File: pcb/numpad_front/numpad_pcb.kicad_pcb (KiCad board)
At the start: 2 copper layers, 56 parts, among them J1 Conn_01x16_Female

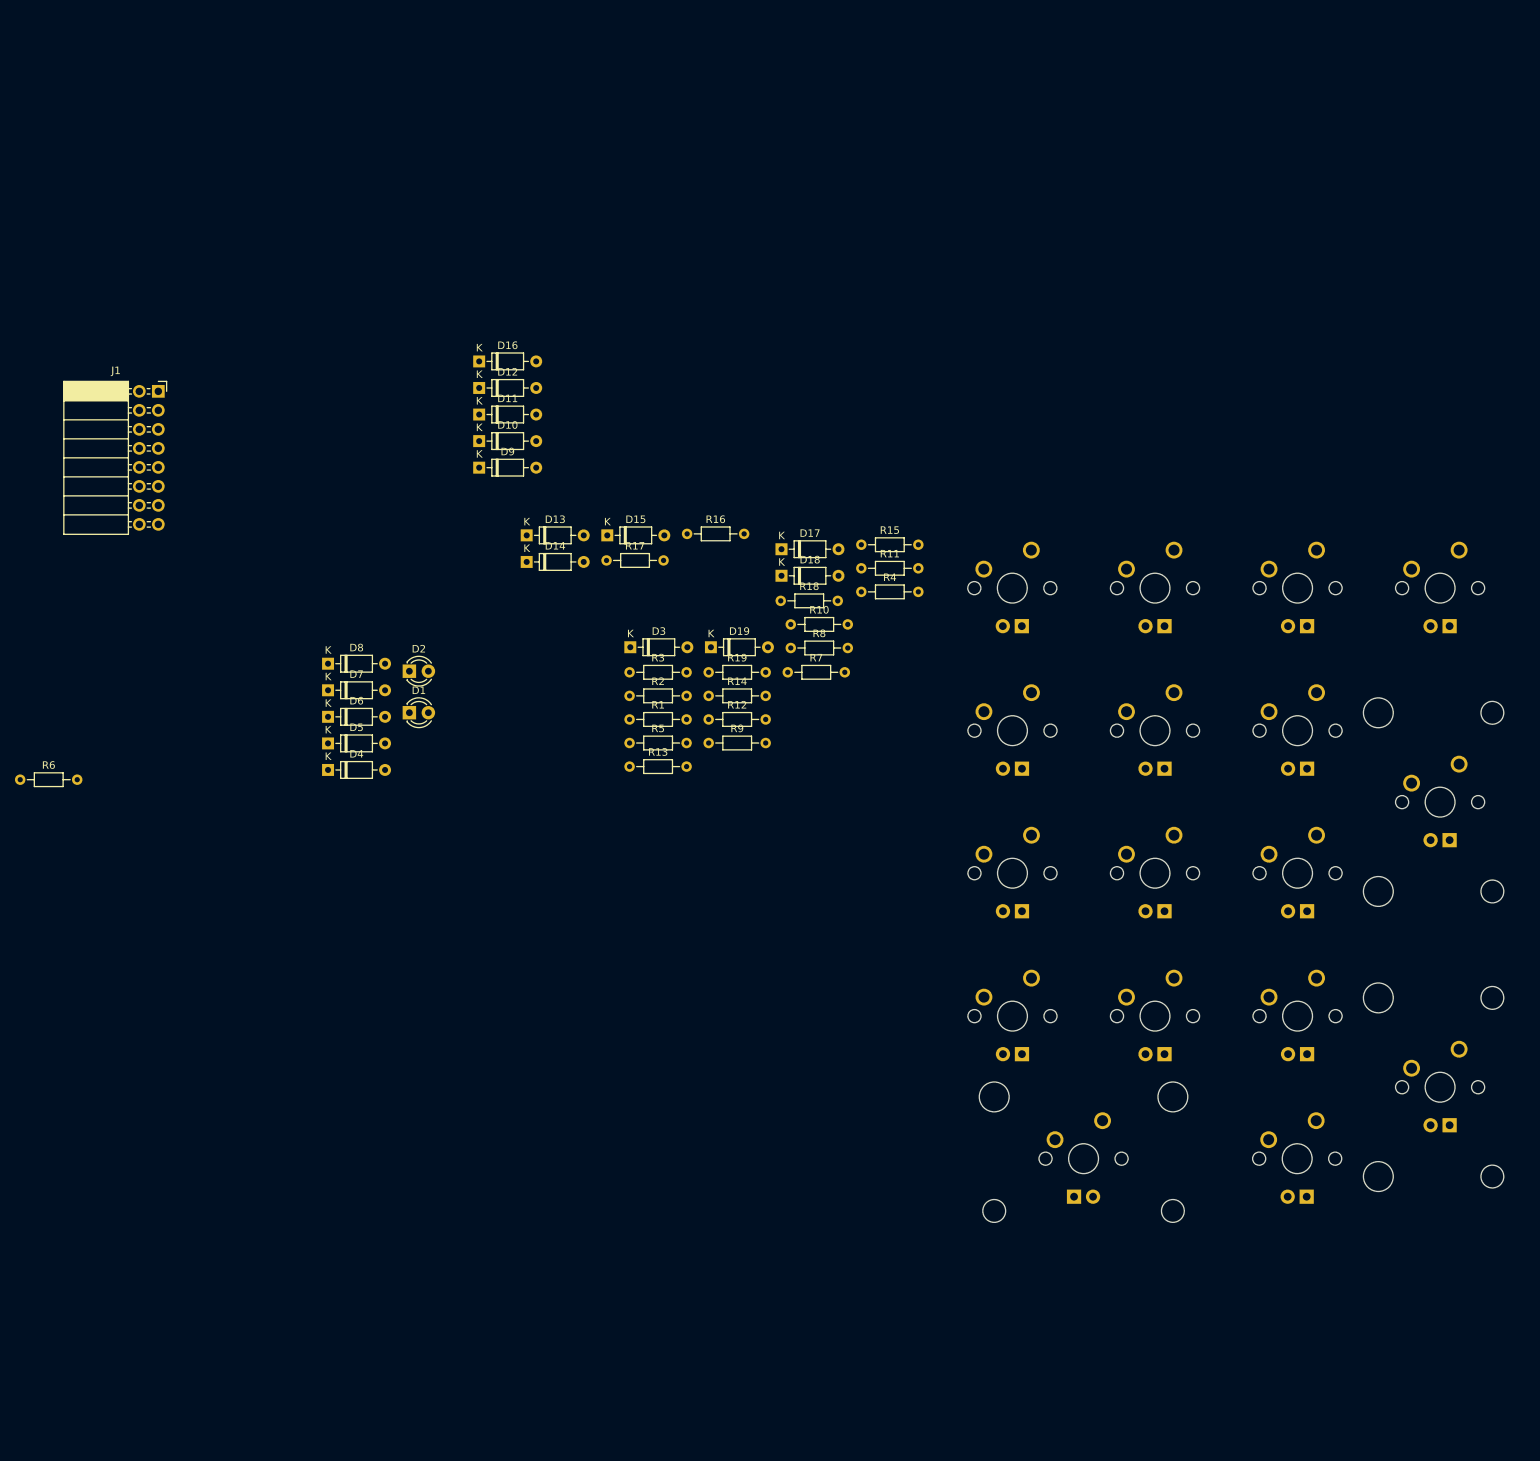
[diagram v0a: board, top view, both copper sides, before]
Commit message: Finish layout for numpad PCB
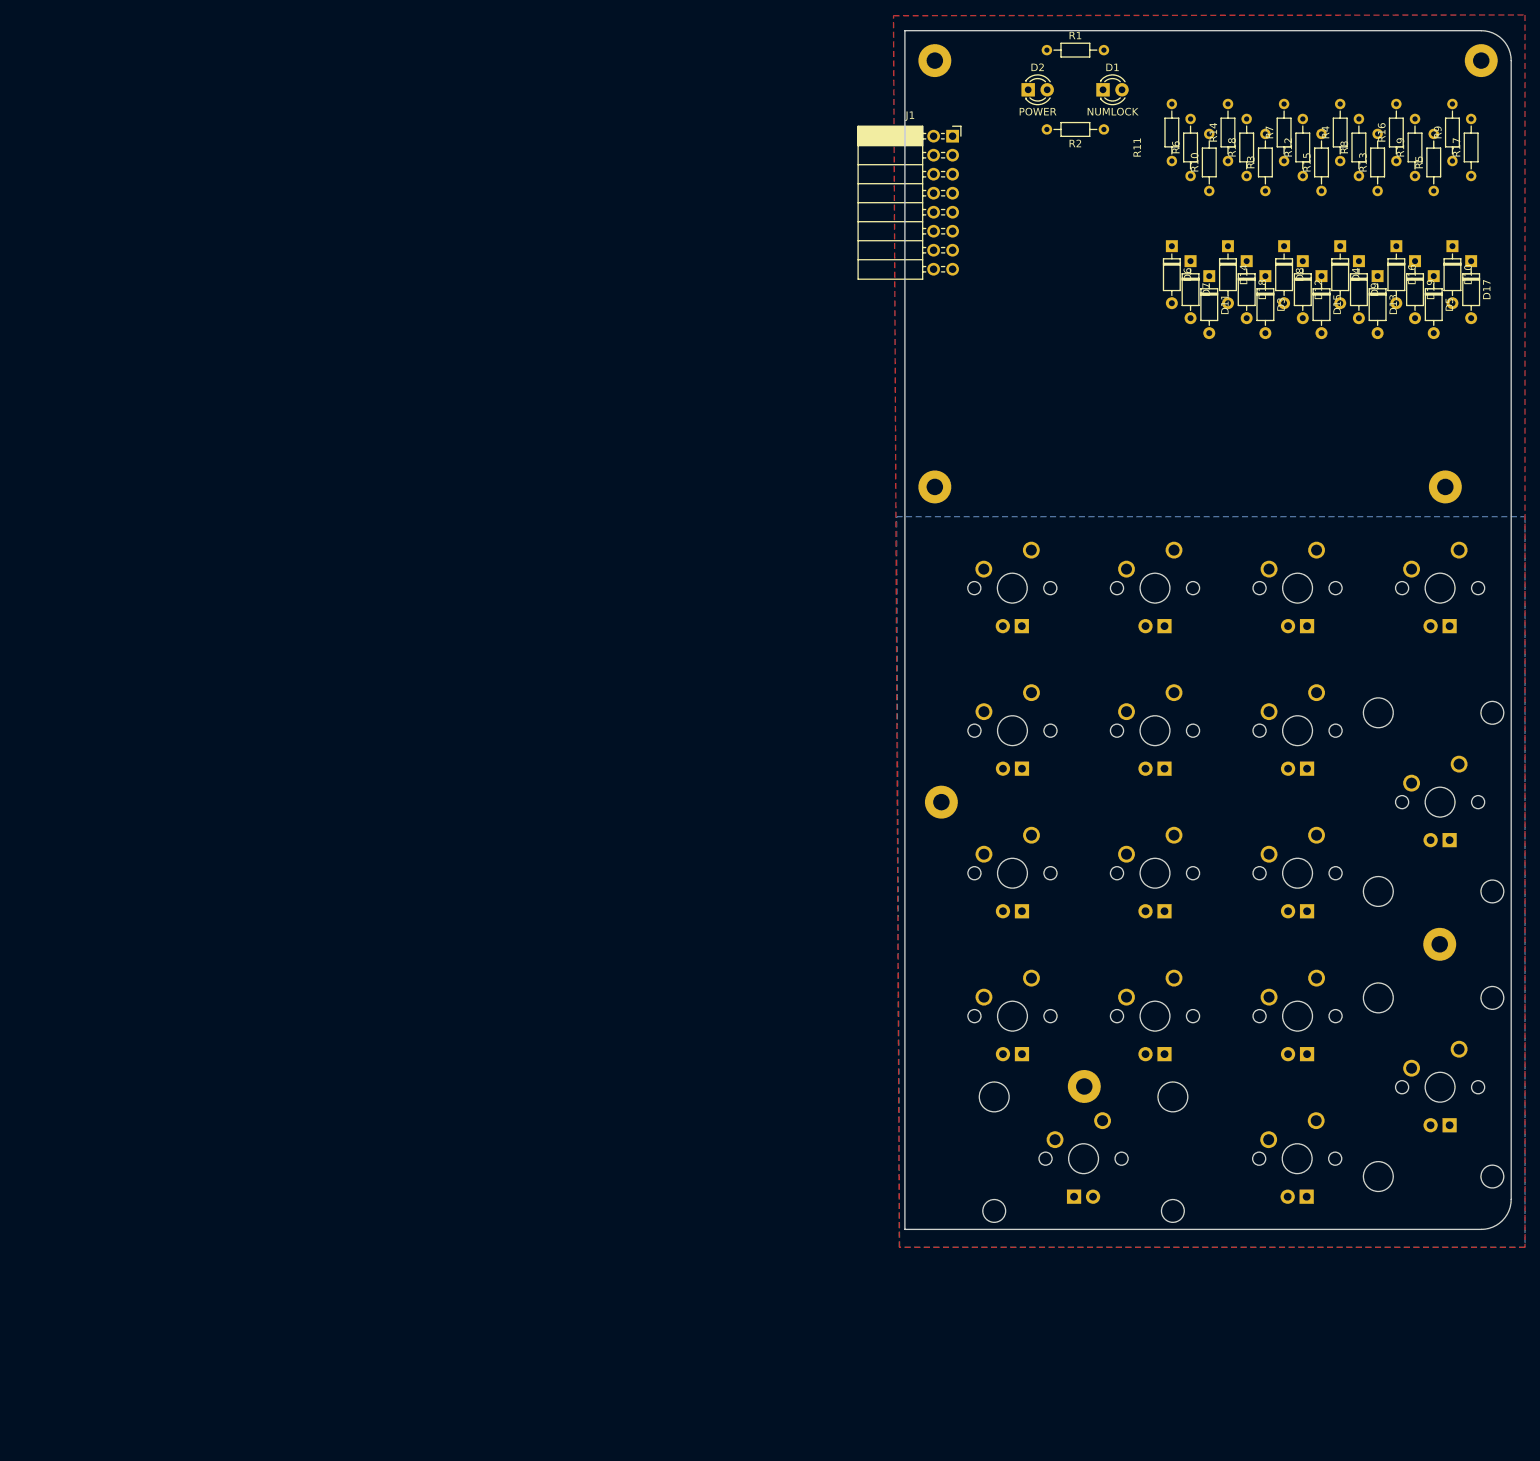
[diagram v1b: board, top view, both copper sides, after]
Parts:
- added REF**: MountingHole_2.2mm_M2_Pad, MountingHole:MountingHole_2.2mm_M2_Pad, F.Cu at (140.5, 3.40)
- added REF** (x2): MountingHole_2.2mm_M2_Pad, MountingHole:MountingHole_2.2mm_M2_Pad, F.Cu at (140.5, 60.4)
- added REF**: MountingHole_2.2mm_M2_Pad, MountingHole:MountingHole_2.2mm_M2_Pad, F.Cu at (141.4, 102.5)
- added REF**: MountingHole_2.2mm_M2_Pad, MountingHole:MountingHole_2.2mm_M2_Pad, F.Cu at (160.5, 140.5)
- added REF**: MountingHole_2.2mm_M2_Pad, MountingHole:MountingHole_2.2mm_M2_Pad, F.Cu at (208.0, 121.5)
- added REF**: MountingHole_2.2mm_M2_Pad, MountingHole:MountingHole_2.2mm_M2_Pad, F.Cu at (213.6, 3.40)
- moved R6 176.0 mm to (174.7, 18.8), turned to 90 degrees
- moved D5 160.4 mm to (207.2, 32.2), turned to 270 degrees
- moved D4 152.3 mm to (194.7, 28.2), turned to 270 degrees
- moved D8 139.4 mm to (187.2, 28.2), turned to 270 degrees
- moved D10 132.7 mm to (209.7, 28.2), turned to 270 degrees
- moved R5 130.4 mm to (207.2, 20.8), turned to 90 degrees
- moved D6 129.1 mm to (172.2, 28.2), turned to 270 degrees
- moved D7 128.7 mm to (174.7, 30.2), turned to 270 degrees
- moved R17 126.5 mm to (212.2, 18.8), turned to 90 degrees
- moved R9 126.2 mm to (209.7, 16.8), turned to 90 degrees
- moved R13 126.1 mm to (199.7, 20.8), turned to 90 degrees
- moved D1 124.6 mm to (163.0, 7.30)
- moved D16 123.5 mm to (202.2, 28.2), turned to 270 degrees
- moved D9 120.8 mm to (197.2, 30.2), turned to 270 degrees
- moved D13 118.9 mm to (199.7, 32.2), turned to 270 degrees
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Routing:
- added copper zone on F.Cu, net GND
- added copper zone on B.Cu, net LEDGND
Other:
- board outline added: 81 x 160.2 mm

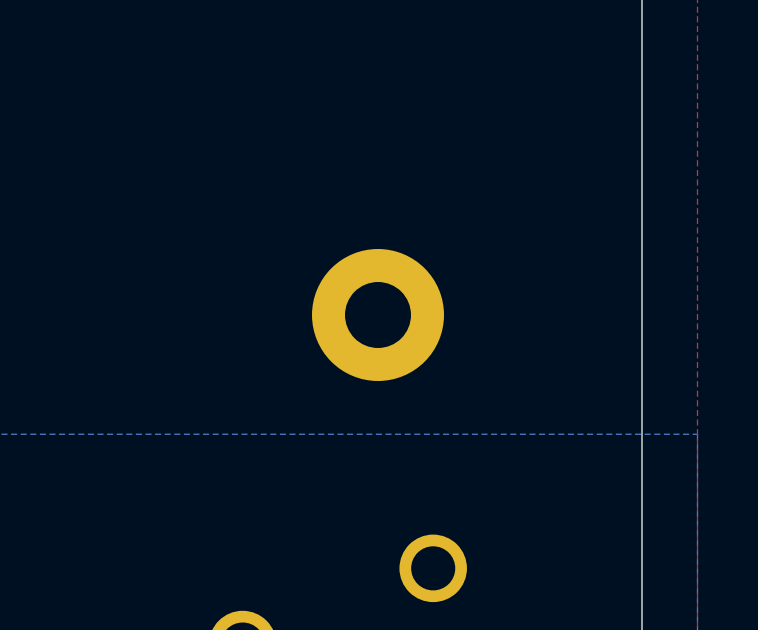
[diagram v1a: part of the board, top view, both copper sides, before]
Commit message: Fix mounting hole
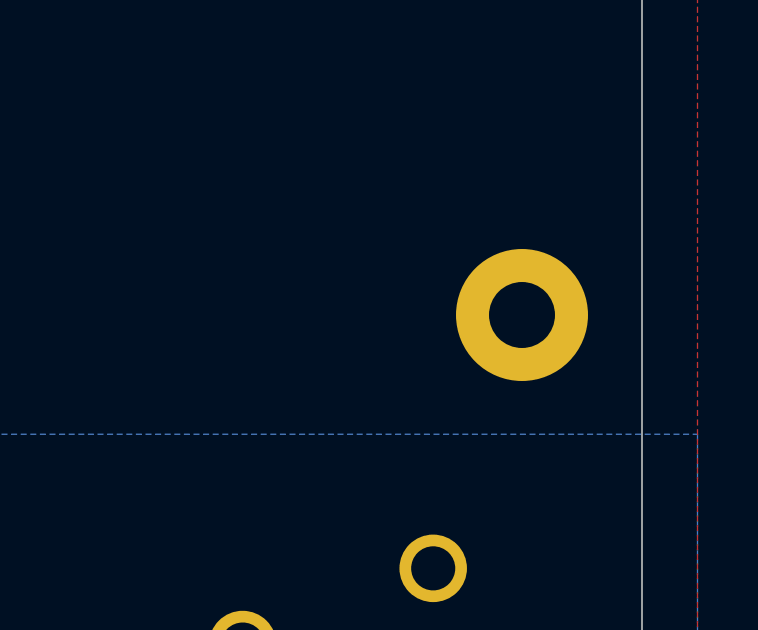
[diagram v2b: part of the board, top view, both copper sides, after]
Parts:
- removed the REF** at (140.5, 60.4) (x2)
- added REF** (x2): MountingHole_2.2mm_M2_Pad, MountingHole:MountingHole_2.2mm_M2_Pad, F.Cu at (140.5, 60.4)
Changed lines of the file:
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@@
     (mod_text_size 1 1)
     (mod_text_width 0.15)
-    (pad_size 1.4 1.4)
-    (pad_drill 0.7)
+    (pad_size 4.4 4.4)
+    (pad_drill 2.2)
     (pad_to_mask_clearance 0.051)
     (solder_mask_min_width 0.25)
@@
       (effects (font (size 1 1) (thickness 0.15)))
     )
-    (pad 1 thru_hole circle (at 68.225 0) (size 4.4 4.4) (drill 2.2) (layers *.Cu *.Mask))
+    (pad 1 thru_hole circle (at 73.025 0) (size 4.4 4.4) (drill 2.2) (layers *.Cu *.Mask))
   )
   (module MountingHole:MountingHole_2.2mm_M2_Pad (layer F.Cu)

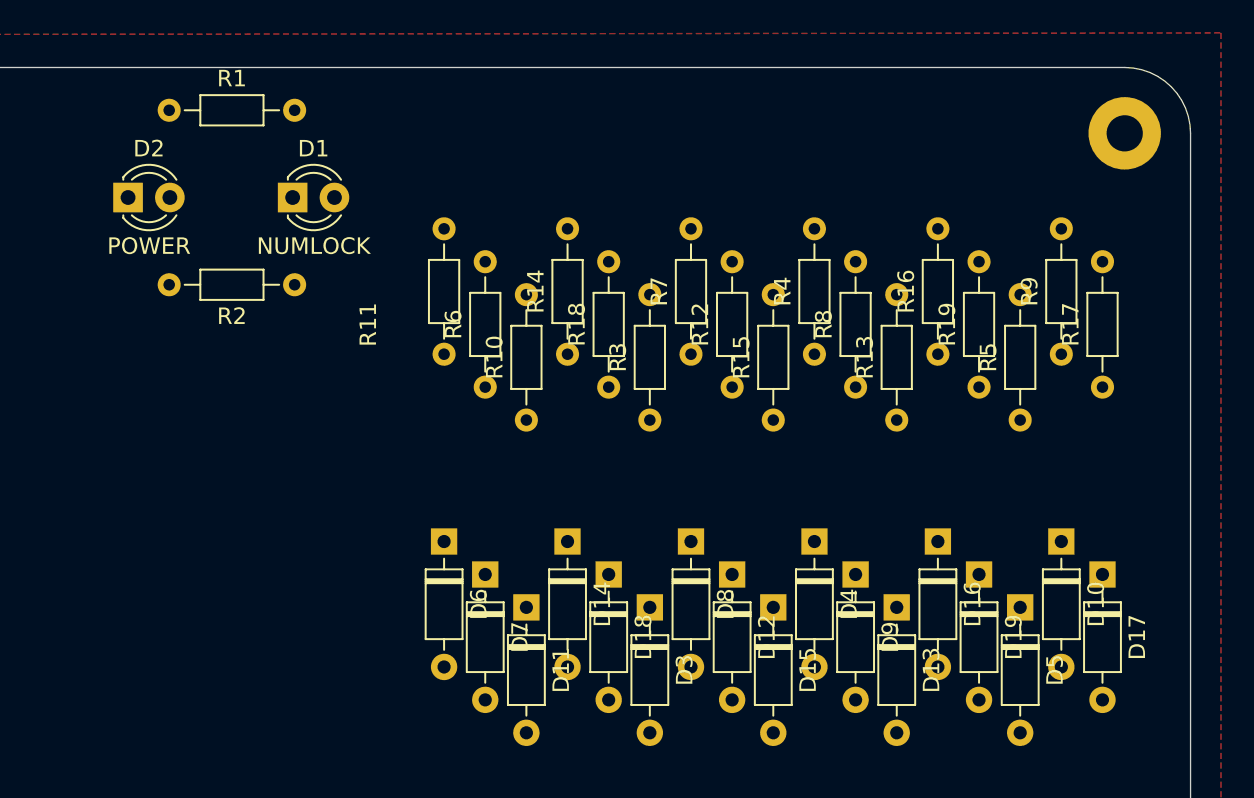
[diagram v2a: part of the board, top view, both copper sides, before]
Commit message: Move silkscreen for numpad
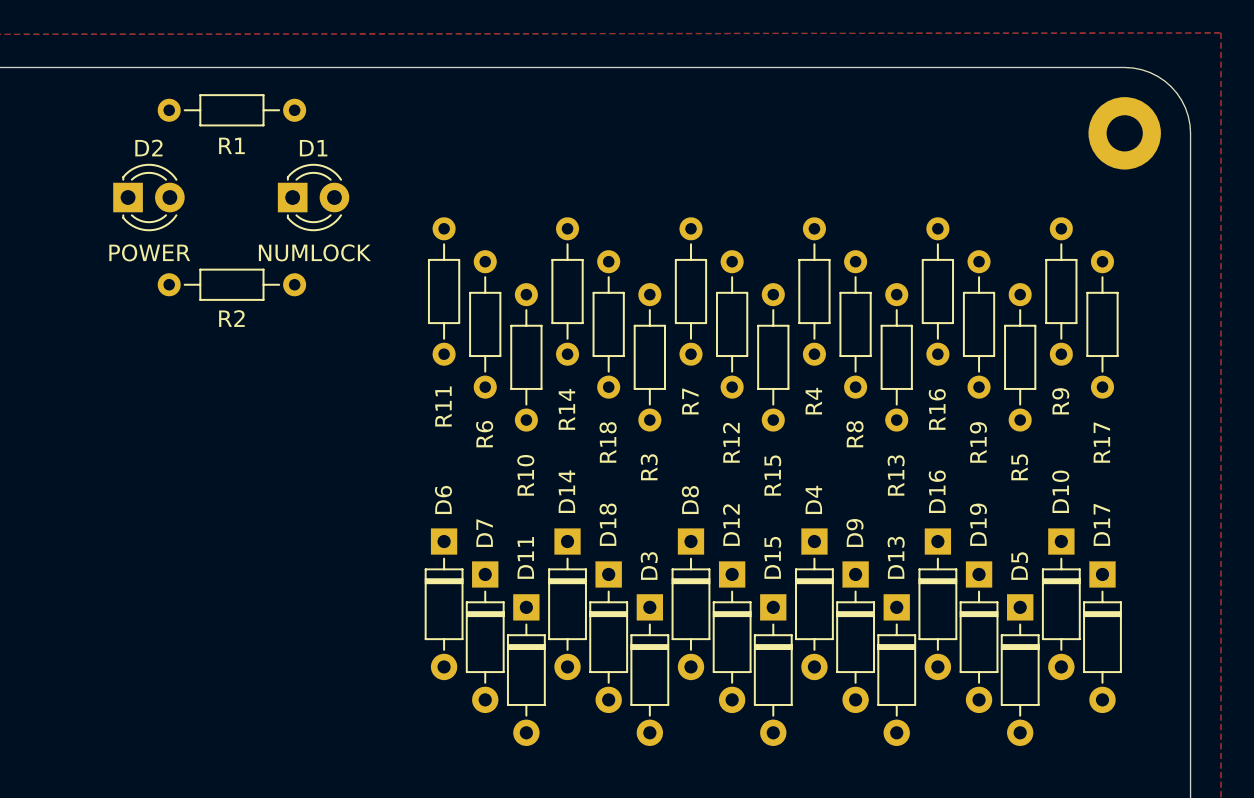
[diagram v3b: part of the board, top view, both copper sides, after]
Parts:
- removed the REF** at (140.5, 60.4) (x2)
- added REF** (x2): MountingHole_2.2mm_M2_Pad, MountingHole:MountingHole_2.2mm_M2_Pad, F.Cu at (140.5, 60.4)

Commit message: Cleanup
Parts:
- removed the REF** at (140.5, 3.40)
- removed the REF** at (140.5, 60.4) (x2)
- removed the REF** at (141.4, 102.5)
- removed the REF** at (160.5, 140.5)
- removed the REF** at (208.0, 121.5)
- removed the REF** at (213.6, 3.40)
- added REF**: MountingHole_2.2mm_M2_Pad, MountingHole:MountingHole_2.2mm_M2_Pad, F.Cu at (67.5, 30.0)
- added REF** (x2): MountingHole_2.2mm_M2_Pad, MountingHole:MountingHole_2.2mm_M2_Pad, F.Cu at (67.5, 87.0)
- added REF**: MountingHole_2.2mm_M2_Pad, MountingHole:MountingHole_2.2mm_M2_Pad, F.Cu at (68.4, 129.1)
- added REF**: MountingHole_2.2mm_M2_Pad, MountingHole:MountingHole_2.2mm_M2_Pad, F.Cu at (87.5, 167.1)
- added REF**: MountingHole_2.2mm_M2_Pad, MountingHole:MountingHole_2.2mm_M2_Pad, F.Cu at (135.0, 148.1)
- added REF**: MountingHole_2.2mm_M2_Pad, MountingHole:MountingHole_2.2mm_M2_Pad, F.Cu at (140.6, 30.0)
- moved D2 100.8 mm to (70.5, 65.2), turned to 180 degrees
- moved R1 91.6 mm to (78.2, 51.2), turned to 270 degrees
- moved R2 91.5 mm to (78.2, 46.7), turned to 90 degrees
- moved D1 87.6 mm to (79.4, 33.6), turned to 180 degrees
- moved D10 77.7 mm to (136.7, 54.8)
- moved D16 77.7 mm to (129.2, 54.8)
- moved D17 77.7 mm to (139.2, 56.8)
- moved D19 77.7 mm to (131.7, 56.8)
- moved D5 77.7 mm to (134.2, 58.8)
- moved J1 77.7 mm to (69.9, 40.1)
- moved MX1 77.7 mm to (77.9, 100.5)
- moved MX11 77.7 mm to (116.0, 138.6)
- moved MX12 77.7 mm to (77.9, 157.7)
- moved MX14 77.7 mm to (116.0, 157.7)
- moved MX15 77.7 mm to (135.1, 167.2)
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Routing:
- added copper zone on F.Cu, net +5V
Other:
- board text added: "NUMPAD CONNECTOR"
